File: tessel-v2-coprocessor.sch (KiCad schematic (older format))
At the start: 37 parts, among them J401 CONN_02X05, J402 USB-micro-TH, J403 MODULE_HEADER, J404 MODULE_HEADER, SW401 SW_PUSH, U401 SAMD21G14A-MU, X401 FC-135

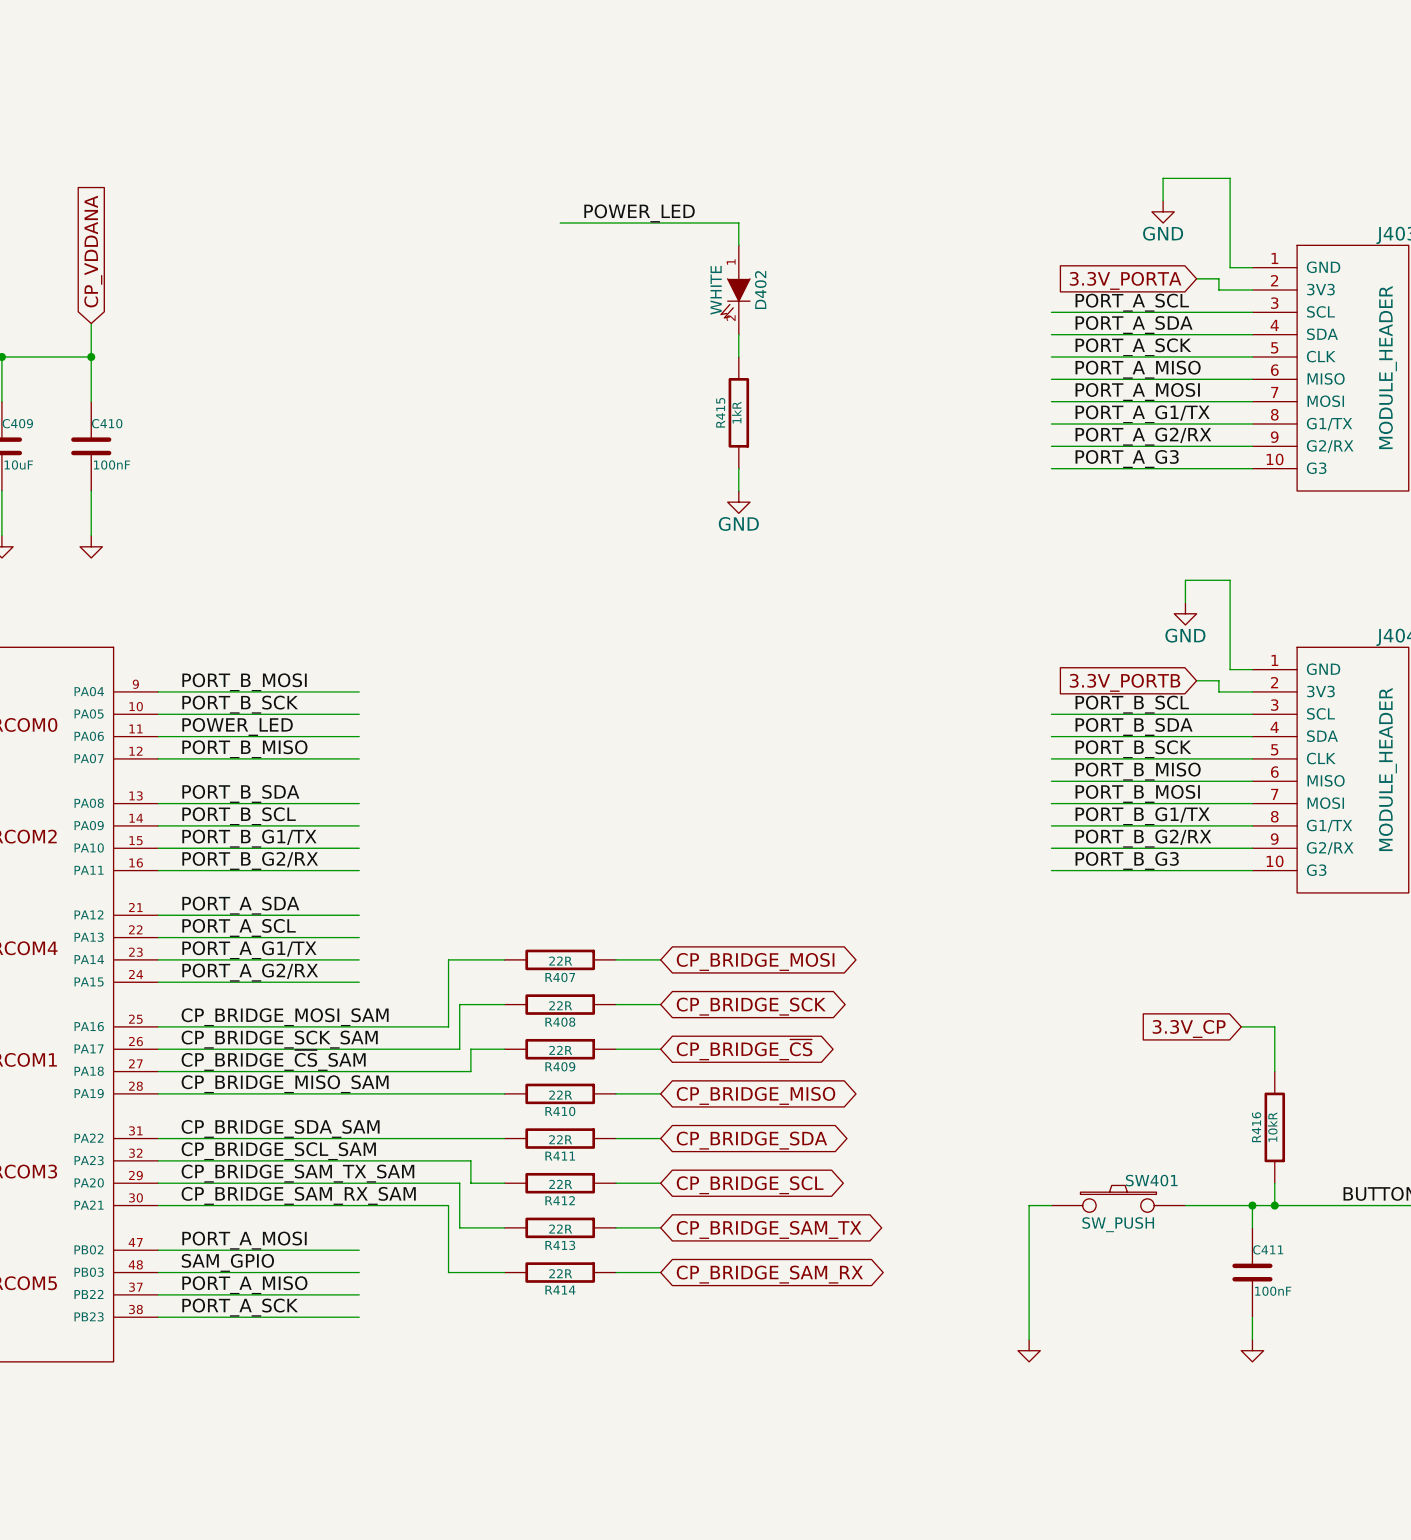
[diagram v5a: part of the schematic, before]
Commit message: fully routed with sca/scl pulls
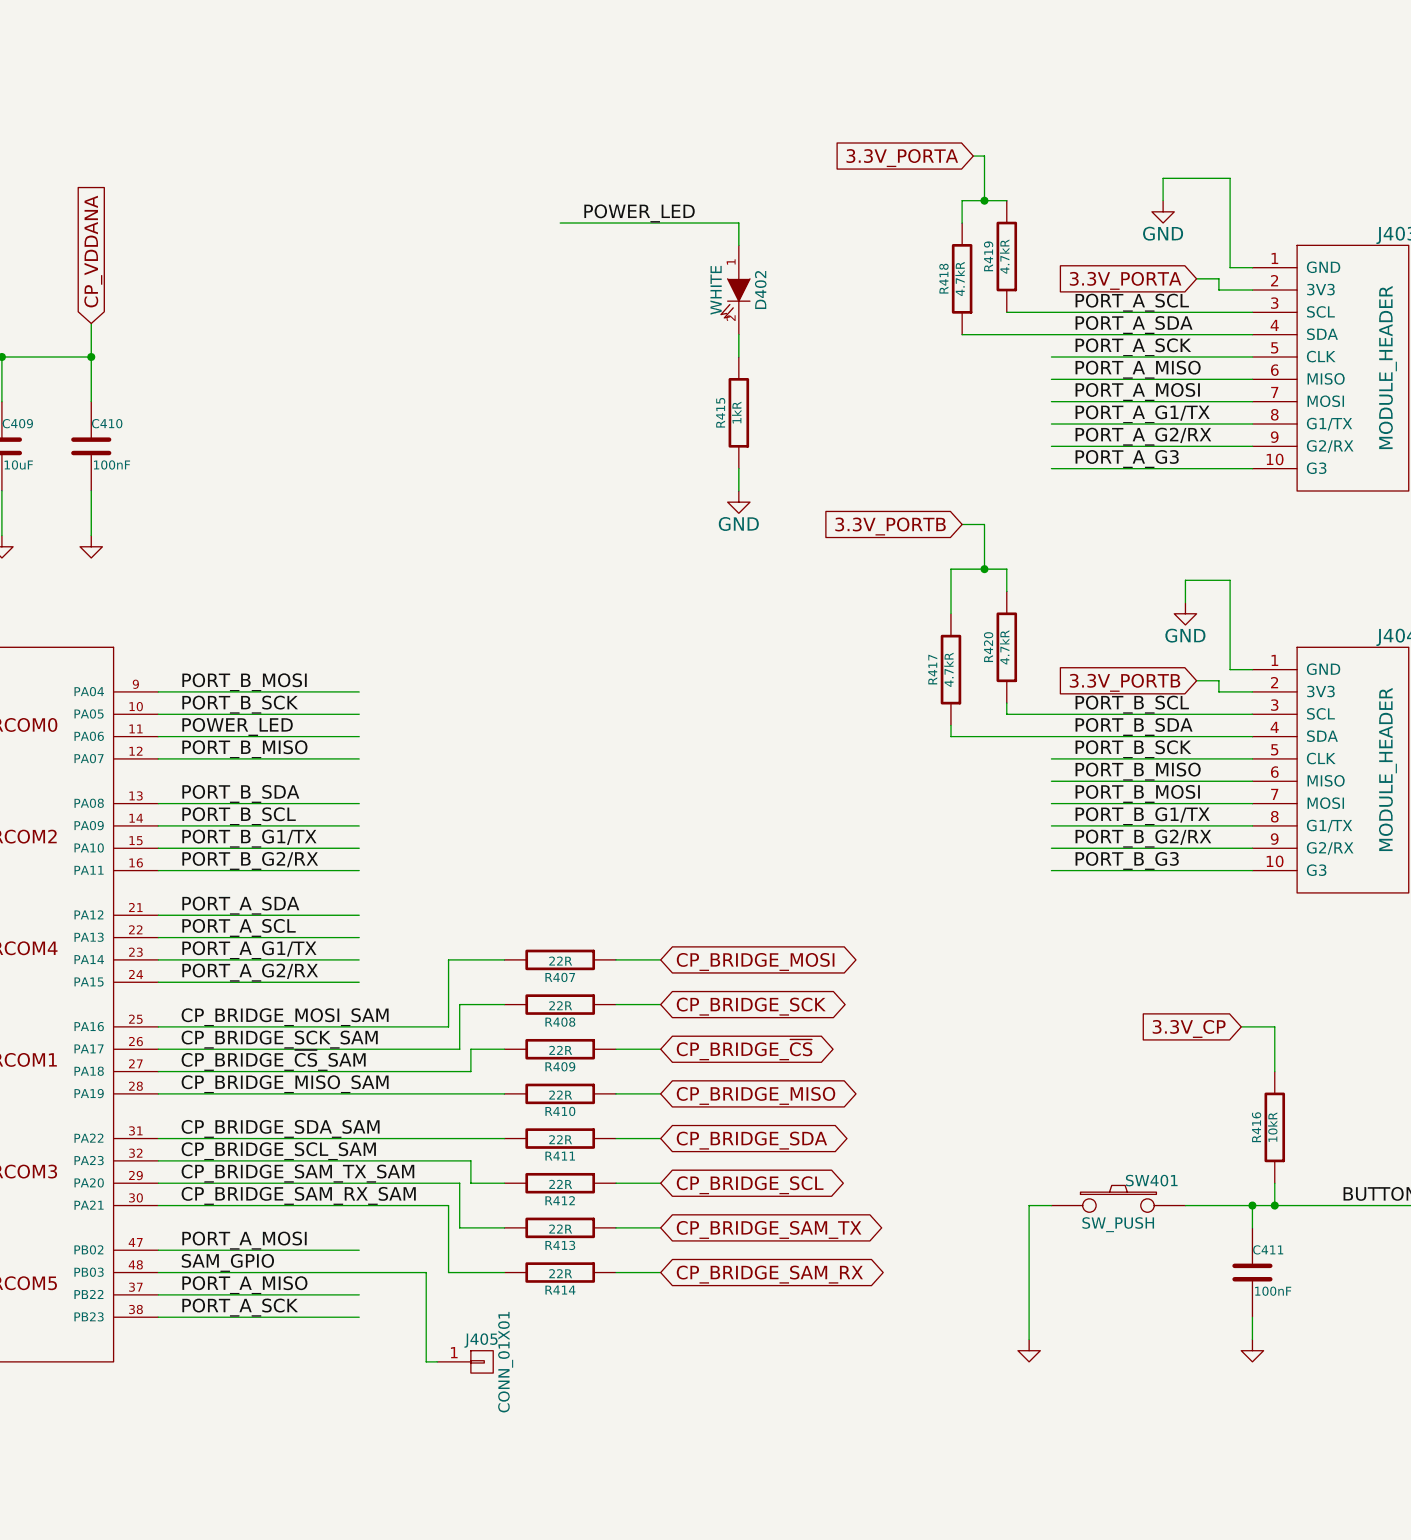
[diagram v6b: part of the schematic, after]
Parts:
- added J405: CONN_01X01, tm-kicad-lib:CONN_01x01_0.05in, symbol CONN_01X01
- added R417, R418, R419, R420: 4.7kR, tm-kicad-lib:SMD-0402-R, symbol R
- J402: footprint tm-kicad-lib:Seeed-USB-Micro-320010028 -> tm-kicad-lib:MICRO-USB-10104111
- J403, J404: footprint tm-kicad-lib:MODULE_HEADER_TESSEL -> tm-kicad-lib:MODULE_HEADER_TESSEL-backside
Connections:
- wire segments 192 -> 205
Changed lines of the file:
@@
 $EndComp
 $Comp
-L GND #PWR0110
+L GND #PWR407
 U 1 1 548F9730
 P 4800 8000
-F 0 "#PWR0110" H 4800 8000 30  0001 C CNN
+F 0 "#PWR407" H 4800 8000 30  0001 C CNN
 F 1 "GND" H 4800 7930 30  0001 C CNN
 F 2 "" H 4800 8000 60  0000 C CNN
@@
 $EndComp
 $Comp
-L GND #PWR0111
+L GND #PWR409
 U 1 1 548F973F
 P 6000 8000
-F 0 "#PWR0111" H 6000 8000 30  0001 C CNN
+F 0 "#PWR409" H 6000 8000 30  0001 C CNN
 F 1 "GND" H 6000 7930 30  0001 C CNN
 F 2 "" H 6000 8000 60  0000 C CNN
@@
 VDDCORE
 $Comp
-L GND #PWR0112
+L GND #PWR416
 U 1 1 548FA205
 P 9400 3900
-F 0 "#PWR0112" H 9400 3900 30  0001 C CNN
+F 0 "#PWR416" H 9400 3900 30  0001 C CNN
 F 1 "GND" H 9400 3830 30  0001 C CNN
 F 2 "" H 9400 3900 60  0000 C CNN
@@
 $EndComp
 $Comp
-L GND #PWR0113
+L GND #PWR415
 U 1 1 548FBD70
 P 9000 3900
-F 0 "#PWR0113" H 9000 3900 30  0001 C CNN
+F 0 "#PWR415" H 9000 3900 30  0001 C CNN
 F 1 "GND" H 9000 3830 30  0001 C CNN
 F 2 "" H 9000 3900 60  0000 C CNN
@@
 $EndComp
 $Comp
-L GND #PWR0114
+L GND #PWR413
 U 1 1 548FBD83
 P 7500 3900
-F 0 "#PWR0114" H 7500 3900 30  0001 C CNN
+F 0 "#PWR413" H 7500 3900 30  0001 C CNN
 F 1 "GND" H 7500 3830 30  0001 C CNN
 F 2 "" H 7500 3900 60  0000 C CNN
@@
 $EndComp
 $Comp
-L GND #PWR0115
+L GND #PWR412
 U 1 1 548FBD8A
 P 7100 3900
-F 0 "#PWR0115" H 7100 3900 30  0001 C CNN
+F 0 "#PWR412" H 7100 3900 30  0001 C CNN
 F 1 "GND" H 7100 3830 30  0001 C CNN
 F 2 "" H 7100 3900 60  0000 C CNN
@@
 $EndComp
 $Comp
-L GND #PWR0116
+L GND #PWR411
 U 1 1 548FBD9D
 P 6700 3900
-F 0 "#PWR0116" H 6700 3900 30  0001 C CNN
+F 0 "#PWR411" H 6700 3900 30  0001 C CNN
 F 1 "GND" H 6700 3830 30  0001 C CNN
 F 2 "" H 6700 3900 60  0000 C CNN
@@
 $EndComp
 $Comp
-L GND #PWR0117
+L GND #PWR410
 U 1 1 548FBDA4
 P 6300 3900
-F 0 "#PWR0117" H 6300 3900 30  0001 C CNN
+F 0 "#PWR410" H 6300 3900 30  0001 C CNN
 F 1 "GND" H 6300 3830 30  0001 C CNN
 F 2 "" H 6300 3900 60  0000 C CNN
@@
 $EndComp
 $Comp
-L GND #PWR0118
+L GND #PWR408
 U 1 1 548FBDB7
 P 5900 3900
-F 0 "#PWR0118" H 5900 3900 30  0001 C CNN
+F 0 "#PWR408" H 5900 3900 30  0001 C CNN
 F 1 "GND" H 5900 3830 30  0001 C CNN
 F 2 "" H 5900 3900 60  0000 C CNN
@@
 $EndComp
 $Comp
-L GND #PWR0119
+L GND #PWR414
 U 1 1 548FD791
 P 8000 8100
-F 0 "#PWR0119" H 8000 8100 30  0001 C CNN
+F 0 "#PWR414" H 8000 8100 30  0001 C CNN
 F 1 "GND" H 8000 8030 30  0001 C CNN
 F 2 "" H 8000 8100 60  0000 C CNN
@@
 $EndComp
 $Comp
-L GND #PWR0120
+L GND #PWR421
 U 1 1 54E6B173
 P 14600 7500
-F 0 "#PWR0120" H 14600 7500 30  0001 C CNN
+F 0 "#PWR421" H 14600 7500 30  0001 C CNN
 F 1 "GND" H 14600 7430 30  0001 C CNN
 F 2 "" H 14600 7500 60  0000 C CNN
@@
 3.3V_CP
 $Comp
-L GND #PWR0121
+L GND #PWR418
 U 1 1 54E6B4A0
 P 13600 7500
-F 0 "#PWR0121" H 13600 7500 30  0001 C CNN
+F 0 "#PWR418" H 13600 7500 30  0001 C CNN
 F 1 "GND" H 13600 7430 30  0001 C CNN
 F 2 "" H 13600 7500 60  0000 C CNN
@@
 NoConn ~ 1700 2700
 $Comp
-L GND #PWR0122
+L GND #PWR402
 U 1 1 54E6D866
 P 1600 2900
-F 0 "#PWR0122" H 1600 2650 60  0001 C CNN
+F 0 "#PWR402" H 1600 2650 60  0001 C CNN
 F 1 "GND" H 1600 2750 60  0000 C CNN
 F 2 "" H 1600 2900 60  0000 C CNN
@@
 3.3V_PORTA
 $Comp
-L GND #PWR0123
+L GND #PWR419
 U 1 1 54E753B7
 P 14200 2400
-F 0 "#PWR0123" H 14200 2150 60  0001 C CNN
+F 0 "#PWR419" H 14200 2150 60  0001 C CNN
 F 1 "GND" H 14200 2250 60  0000 C CNN
 F 2 "" H 14200 2400 60  0000 C CNN
@@
 $EndComp
 $Comp
-L GND #PWR0124
+L GND #PWR420
 U 1 1 54E753CD
 P 14300 4200
-F 0 "#PWR0124" H 14300 3950 60  0001 C CNN
+F 0 "#PWR420" H 14300 3950 60  0001 C CNN
 F 1 "GND" H 14300 4050 60  0000 C CNN
 F 2 "" H 14300 4200 60  0000 C CNN
@@
 F 0 "J404" H 14550 5450 60  0000 C CNN
 F 1 "MODULE_HEADER" V 14600 4850 60  0000 C CNN
-F 2 "tm-kicad-lib:MODULE_HEADER_TESSEL" H 14900 4900 60  0001 C CNN
+F 2 "tm-kicad-lib:MODULE_HEADER_TESSEL-backside" H 14900 4900 60  0001 C CNN
 F 3 "" H 14900 4900 60  0000 C CNN
 	1    14900 4900
@@
 F 0 "J403" H 14550 3650 60  0000 C CNN
 F 1 "MODULE_HEADER" V 14600 3050 60  0000 C CNN
-F 2 "tm-kicad-lib:MODULE_HEADER_TESSEL" H 14900 3100 60  0001 C CNN
+F 2 "tm-kicad-lib:MODULE_HEADER_TESSEL-backside" H 14900 3100 60  0001 C CNN
 F 3 "" H 14900 3100 60  0000 C CNN
 	1    14900 3100
@@
 PORT_A_G3
 $Comp
-L +5V #PWR0125
+L +5V #PWR403
 U 1 1 54E79A0D
 P 2800 3900
-F 0 "#PWR0125" H 2800 3990 20  0001 C CNN
+F 0 "#PWR403" H 2800 3990 20  0001 C CNN
 F 1 "+5V" H 2800 4050 30  0000 C CNN
 F 2 "" H 2800 3900 60  0000 C CNN
@@
 $EndComp
 $Comp
-L GND #PWR0126
+L GND #PWR404
 U 1 1 54E79A13
 P 2800 4600
-F 0 "#PWR0126" H 2800 4350 60  0001 C CNN
+F 0 "#PWR404" H 2800 4350 60  0001 C CNN
 F 1 "GND" H 2800 4450 60  0000 C CNN
 F 2 "" H 2800 4600 60  0000 C CNN
@@
 $EndComp
 $Comp
-L GND #PWR0127
+L GND #PWR405
 U 1 1 54E79A19
 P 3100 5000
-F 0 "#PWR0127" H 3100 4750 60  0001 C CNN
+F 0 "#PWR405" H 3100 4750 60  0001 C CNN
 F 1 "GND" H 3100 4850 60  0000 C CNN
 F 2 "" H 3100 5000 60  0000 C CNN
@@
 $EndComp
 $Comp
-L GND #PWR0128
+L GND #PWR401
 U 1 1 54E79A1F
 P 1500 5500
-F 0 "#PWR0128" H 1500 5250 60  0001 C CNN
+F 0 "#PWR401" H 1500 5250 60  0001 C CNN
 F 1 "GND" H 1500 5350 60  0000 C CNN
 F 2 "" H 1500 5500 60  0000 C CNN
@@
 $EndComp
 $Comp
-L +5V #PWR0129
+L +5V #PWR406
 U 1 1 54E79A2D
 P 4000 4600
-F 0 "#PWR0129" H 4000 4690 20  0001 C CNN
+F 0 "#PWR406" H 4000 4690 20  0001 C CNN
 F 1 "+5V" H 4000 4750 30  0000 C CNN
 F 2 "" H 4000 4600 60  0000 C CNN
@@
 F 0 "J402" H 1900 4650 60  0000 C CNN
 F 1 "USB-micro-TH" H 2200 4550 60  0000 C CNN
-F 2 "tm-kicad-lib:Seeed-USB-Micro-320010028" H 2300 4200 60  0001 C CNN
+F 2 "tm-kicad-lib:MICRO-USB-10104111" H 2300 4200 60  0001 C CNN
 F 3 "" H 2300 4200 60  0000 C CNN
 	1    2300 4200
@@
 FLASH_~CS
 $Comp
-L GND #PWR0130
+L GND #PWR417
 U 1 1 54EE1D18
 P 12300 3700
-F 0 "#PWR0130" H 12300 3450 60  0001 C CNN
+F 0 "#PWR417" H 12300 3450 60  0001 C CNN
 F 1 "GND" H 12300 3550 60  0000 C CNN
 F 2 "" H 12300 3700 60  0000 C CNN
@@
 Text Label 5700 5700 0    60   ~ 0
 ~PORST~_SAM
+Text Notes 4750 8300 0    60   ~ 0
+load cap derated from 12.5pF
+Text Notes 5250 7800 0    60   ~ 0
+12.5pF\nNOMINAL\nSHUNT
+$Comp
+L CONN_01X01 J405
+U 1 1 54F518CE
+P 11150 7600
+F 0 "J405" H 11150 7700 50  0000 C CNN
+F 1 "CONN_01X01" V 11250 7600 50  0000 C CNN
+F 2 "tm-kicad-lib:CONN_01x01_0.05in" H 11150 7600 60  0001 C CNN
+F 3 "" H 11150 7600 60  0000 C CNN
+	1    11150 7600
+	1    0    0    -1
+$EndComp
+$Comp
+L R R419
+U 1 1 54F4EEC1
+P 13500 2650
+F 0 "R419" V 13580 2650 40  0000 C CNN
+F 1 "4.7kR" V 13507 2651 40  0000 C CNN
+F 2 "tm-kicad-lib:SMD-0402-R" V 13430 2650 30  0001 C CNN
+F 3 "" H 13500 2650 30  0000 C CNN
+	1    13500 2650
+	-1   0    0    1
+$EndComp
+$Comp
+L R R418
+U 1 1 54F4EF88
+P 13300 2750
+F 0 "R418" V 13380 2750 40  0000 C CNN
+F 1 "4.7kR" V 13307 2751 40  0000 C CNN
+F 2 "tm-kicad-lib:SMD-0402-R" V 13230 2750 30  0001 C CNN
+F 3 "" H 13300 2750 30  0000 C CNN
+	1    13300 2750
+	-1   0    0    1
+$EndComp
 Wire Wire Line
 	4000 4700 4000 4600
@@
 	14600 4900 13700 4900
 Wire Wire Line
-	14600 4800 13700 4800
-Wire Wire Line
-	14600 4700 13700 4700
+	13250 4800 14600 4800
+Wire Wire Line
+	13500 4700 14600 4700
 Wire Wire Line
 	14600 3600 13700 3600
@@
 	14600 3100 13700 3100
 Wire Wire Line
-	14600 3000 13700 3000
-Wire Wire Line
-	14600 2900 13700 2900
+	13300 3000 14600 3000
+Wire Wire Line
+	13500 2900 14600 2900
 Wire Wire Line
 	14450 4600 14600 4600
@@
 	4950 6550 5100 6550
 Wire Wire Line
-	9700 7200 10600 7200
+	9700 7200 10900 7200
 Wire Wire Line
 	9700 4800 10600 4800
@@
 	5500 4600 5500 4700
 Connection ~ 5500 4700
-Text Notes 4750 8300 0    60   ~ 0
-load cap derated from 12.5pF
-Text Notes 5250 7800 0    60   ~ 0
-12.5pF\nNOMINAL\nSHUNT
+Wire Wire Line
+	10900 7200 10900 7600
+Wire Wire Line
+	10900 7600 10950 7600
+Wire Wire Line
+	13500 2400 13300 2400
+Wire Wire Line
+	13300 2400 13300 2500
+Text GLabel 13350 2200 0    60   Input ~ 0
+3.3V_PORTA
+Wire Wire Line
+	13350 2200 13400 2200
+Wire Wire Line
+	13400 2200 13400 2400
+Connection ~ 13400 2400
+$Comp
+L R R420
+U 1 1 54F4F7D9
+P 13500 4400
+F 0 "R420" V 13580 4400 40  0000 C CNN
+F 1 "4.7kR" V 13507 4401 40  0000 C CNN
+F 2 "tm-kicad-lib:SMD-0402-R" V 13430 4400 30  0001 C CNN
+F 3 "" H 13500 4400 30  0000 C CNN
+	1    13500 4400
+	-1   0    0    1
+$EndComp
+$Comp
+L R R417
+U 1 1 54F4F93B
+P 13250 4500
+F 0 "R417" V 13330 4500 40  0000 C CNN
+F 1 "4.7kR" V 13257 4501 40  0000 C CNN
+F 2 "tm-kicad-lib:SMD-0402-R" V 13180 4500 30  0001 C CNN
+F 3 "" H 13250 4500 30  0000 C CNN
+	1    13250 4500
+	-1   0    0    1
+$EndComp
+Wire Wire Line
+	13500 4650 13500 4700
+Wire Wire Line
+	13250 4800 13250 4750
+Wire Wire Line
+	13250 4250 13250 4050
+Wire Wire Line
+	13250 4050 13500 4050
+Wire Wire Line
+	13500 4050 13500 4150
+Text GLabel 13300 3850 0    60   Input ~ 0
+3.3V_PORTB
+Wire Wire Line
+	13300 3850 13400 3850
+Wire Wire Line
+	13400 3850 13400 4050
+Connection ~ 13400 4050
 $EndSCHEMATC

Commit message: cleaned up schematics for release (tm-t2-03)
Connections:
- wire segments 205 -> 239
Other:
- moved on the sheet: D402, J405, R415, R417, R418, R419, R420
